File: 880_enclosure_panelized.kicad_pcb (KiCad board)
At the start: 4 copper layers, 279.5 x 38 mm, 161 parts, among them CON1 BARREL_JACK, J1 RUN/STOP, J10 RS IN, J11 CP IN, J12 MA IN, J13 CB IN, J14 CY IN, J15 OH IN, J16 CH IN, J17 IN 1, J18 IN 2, J19 IN 3, J2 SYNC24 CLK, J20 IN 4, J21 MULT IN, J22 SUM, J3 ASSIGN 1, J4 ASSIGN 2, J5 BD IN, J6 SD IN, J7 LT IN, J8 MT IN, J9 HT IN, P1 CONN_02X03, P2 CONN_01X02, P3 CONN_02X08, P4 CONN_01X03, P5 CONN_01X04, P7 CONN_01X03, Q1 MMBT3904, Q10 MMBT3904, Q11 MMBT3904, Q12 MMBT3904, Q14 C945, Q15 A733, Q2 MMBT3904, Q3 MMBT3904, Q4 MMBT3904, Q5 MMBT3904, Q6 MMBT3904, Q7 MMBT3904, Q8 MMBT3904, Q9 MMBT3904, U1 74HC165, U2 74HC165, U3 VX078-500, U4 VX078-500, U5 4558, U6 4558, U7 74HC1G125, X1 MIDI OUT, X2 SYNC24

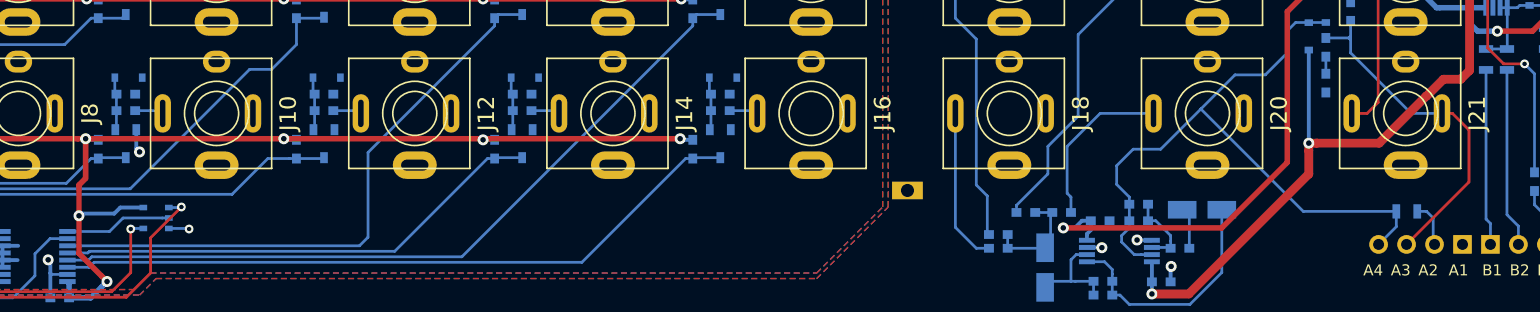
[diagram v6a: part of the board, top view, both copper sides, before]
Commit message: 4 layer, added tri-state buffer on MISO line, ordered prototype PCB
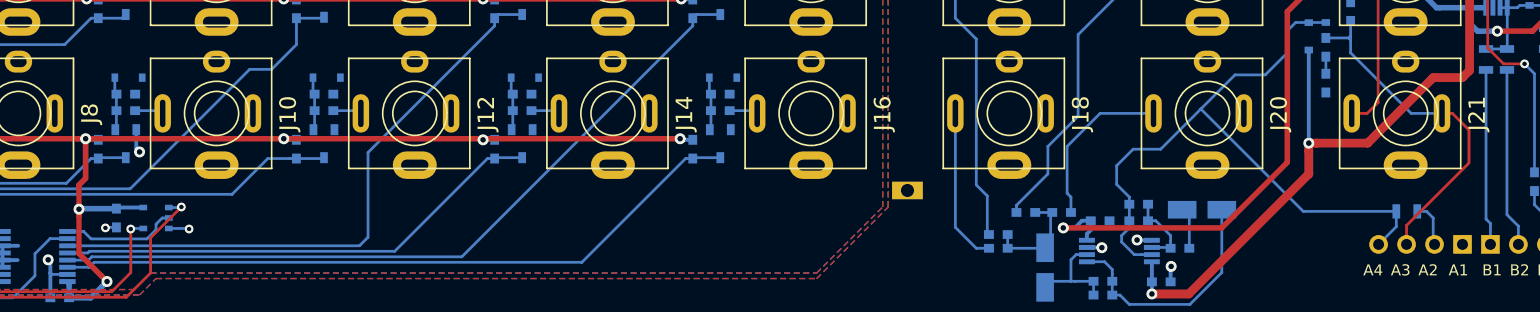
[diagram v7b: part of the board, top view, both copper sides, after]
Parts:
- added C20: 0.1µ, MyModules:SM0603-C-MURATA, B.Cu at (141.9, 86.5)
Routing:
- net GNDD: track 78.9 -> 79.9 mm, vias 6 -> 7
- net Net-(U2-Pad9): track 9.74 -> 10.6 mm
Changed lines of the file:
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@@
 (kicad_pcb (version 4) (host pcbnew 4.0.2-stable)
   (general
-    (links 349)
+    (links 351)
     (no_connects 0)
-    (area 11.944431 57.449999 291.550001 95.551147)
+    (area 9.341667 55.389285 291.550001 97.0016)
     (thickness 1.6)
     (drawings 115)
-    (tracks 798)
+    (tracks 804)
     (zones 0)
-    (modules 161)
+    (modules 162)
     (nets 111)
   )
@@
     (35 F.Paste user)
     (36 B.SilkS user)
-    (37 F.SilkS user hide)
+    (37 F.SilkS user)
     (38 B.Mask user)
     (39 F.Mask user)
@@
   )
   (setup
-    (last_trace_width 0.35)
+    (last_trace_width 0.25)
     (user_trace_width 0.25)
     (user_trace_width 0.35)
@@
     (visible_elements 7FFFF77F)
     (pcbplotparams
-      (layerselection 0x010f0_80000001)
+      (layerselection 0x010f0_80000007)
       (usegerberextensions true)
       (excludeedgelayer true)
@@
       (drillshape 0)
       (scaleselection 1)
-      (outputdirectory Gerbers/))
+      (outputdirectory Gerbers/r1.2/))
   )
   (net 0 "")
@@
     )
   )
+  (module MyModules:SM0603-C-MURATA (layer B.Cu)
+    (at 141.9 86.5 270)
+    (attr smd)
+    (fp_text reference C20 (at 0 1.4 270) (layer B.SilkS)
+      (effects (font (size 0.6096 0.6096) (thickness 0.1524)) (justify mirror))
+    )
+    (fp_text value 0.1µ (at 0 0 270) (layer B.SilkS) hide
+      (effects (font (size 0.508 0.4572) (thickness 0.1143)) (justify mirror))
+    )
+    (fp_line (start -0.5 0.5) (end 0.5 0.5) (layer B.SilkS) (width 0.2))
+    (fp_line (start -0.5 -0.5) (end 0.5 -0.5) (layer B.SilkS) (width 0.2))
+    (pad 1 smd rect (at -0.85 0 270) (size 0.9 0.8) (layers B.Cu B.Paste B.Mask)
+      (net 3 +5V))
+    (pad 2 smd rect (at 0.85 0 270) (size 0.9 0.8) (layers B.Cu B.Paste B.Mask)
+      (net 106 GNDD))
+    (model Capacitors_SMD.3dshapes/C_0603.wrl
+      (at (xyz 0 0 0.001))
+      (scale (xyz 1 1 1))
+      (rotate (xyz 0 0 0))
+    )
+  )
   (gr_text GND (at 75 92.5) (layer B.SilkS)
     (effects (font (size 0.8 0.8) (thickness 0.15)) (justify mirror))
@@
   (segment (start 30.4 83.3) (end 28.6 83.3) (width 0.35) (layer B.Cu) (net 2))
   (via (at 28.6 83.3) (size 1) (drill 0.5) (layers F.Cu B.Cu) (net 2))
+  (segment (start 138.5 83.5) (end 138.5 85.7) (width 0.5) (layer F.Cu) (net 3))
+  (segment (start 138.5 85.7) (end 138.5 86.3) (width 0.5) (layer F.Cu) (net 3))
+  (via (at 138.5 85.7) (size 1) (drill 0.5) (layers F.Cu B.Cu) (net 3))
+  (segment (start 141.9 85.65) (end 138.55 85.65) (width 0.5) (layer B.Cu) (net 3))
+  (segment (start 138.55 85.65) (end 138.5 85.7) (width 0.35) (layer B.Cu) (net 3))
+  (segment (start 144.34 85.55) (end 142 85.55) (width 0.35) (layer B.Cu) (net 3))
+  (segment (start 142 85.55) (end 141.9 85.65) (width 0.35) (layer B.Cu) (net 3))
   (segment (start 138.5 89.721069) (end 140.548913 91.769982) (width 0.5) (layer F.Cu) (net 3))
   (segment (start 140.548913 92.76998) (end 141.048912 92.269981) (width 0.5) (layer B.Cu) (net 3))
@@
   (segment (start 137.6 93.75) (end 137.6 92.425) (width 0.5) (layer B.Cu) (net 3))
   (segment (start 137.6 92.425) (end 137.525001 92.350001) (width 0.5) (layer B.Cu) (net 3))
-  (segment (start 138.5 83.5) (end 138.5 86.3) (width 0.5) (layer F.Cu) (net 3))
   (segment (start 139.1 79.3) (end 139.1 82.9) (width 0.5) (layer F.Cu) (net 3))
   (segment (start 139.1 82.9) (end 138.5 83.5) (width 0.5) (layer F.Cu) (net 3))
-  (segment (start 144.34 85.55) (end 142.25 85.55) (width 0.35) (layer B.Cu) (net 3))
-  (segment (start 142.25 85.55) (end 141.7 86.1) (width 0.35) (layer B.Cu) (net 3))
-  (segment (start 141.7 86.1) (end 138.7 86.1) (width 0.35) (layer B.Cu) (net 3))
-  (segment (start 138.7 86.1) (end 138.5 86.3) (width 0.35) (layer B.Cu) (net 3))
-  (via (at 138.5 86.3) (size 1) (drill 0.5) (layers F.Cu B.Cu) (net 3))
   (segment (start 120.5 76.7) (end 122.2 76.7) (width 0.8) (layer B.Cu) (net 3))
   (segment (start 122.2 76.7) (end 122.25 76.75) (width 0.35) (layer B.Cu) (net 3))
@@
   (segment (start 67.4505 88.9205) (end 67.53 89) (width 1) (layer B.Cu) (net 8))
   (segment (start 67.53 89) (end 70.95 89) (width 1) (layer B.Cu) (net 8))
+  (segment (start 271.500002 59.4) (end 267.4 59.4) (width 0.8) (layer F.Cu) (net 9))
+  (segment (start 267.4 59.4) (end 264.8 62) (width 0.8) (layer F.Cu) (net 9))
+  (segment (start 264.8 62) (end 264.8 73.1) (width 0.8) (layer F.Cu) (net 9))
+  (segment (start 264.8 73.1) (end 264.15 73.75) (width 0.8) (layer F.Cu) (net 9))
+  (segment (start 264.15 73.75) (end 261.5 73.75) (width 0.8) (layer F.Cu) (net 9))
+  (segment (start 261.5 73.75) (end 255.55 79.7) (width 0.8) (layer F.Cu) (net 9))
+  (segment (start 255.55 79.7) (end 250.907112 79.7) (width 0.8) (layer F.Cu) (net 9))
+  (segment (start 250.907112 79.7) (end 250.200006 79.7) (width 0.8) (layer F.Cu) (net 9))
   (segment (start 41.23 88.98) (end 41.23 87.27) (width 1) (layer In1.Cu) (net 9))
   (segment (start 70.8 83.4) (end 74.5 87.1) (width 1) (layer In1.Cu) (net 9))
@@
   (segment (start 29.1795 89.3205) (end 33.4 85.1) (width 1) (layer B.Cu) (net 9))
   (segment (start 33.4 85.1) (end 33.4 83.3) (width 1) (layer B.Cu) (net 9))
-  (segment (start 271.500002 59.4) (end 267.4 59.4) (width 0.8) (layer F.Cu) (net 9))
-  (segment (start 267.4 59.4) (end 264.8 62) (width 0.8) (layer F.Cu) (net 9))
-  (segment (start 264.8 62) (end 264.8 73.1) (width 0.8) (layer F.Cu) (net 9))
-  (segment (start 264.8 73.1) (end 264 73.9) (width 0.8) (layer F.Cu) (net 9))
-  (segment (start 264 73.9) (end 262.420087 73.9) (width 0.8) (layer F.Cu) (net 9))
-  (segment (start 262.420087 73.9) (end 260.89999 75.420097) (width 0.8) (layer F.Cu) (net 9))
-  (segment (start 260.89999 75.420097) (end 260.879903 75.420097) (width 0.8) (layer F.Cu) (net 9))
-  (segment (start 260.879903 75.420097) (end 256.6 79.7) (width 0.8) (layer F.Cu) (net 9))
-  (segment (start 256.6 79.7) (end 250.907112 79.7) (width 0.8) (layer F.Cu) (net 9))
-  (segment (start 250.907112 79.7) (end 250.200006 79.7) (width 0.8) (layer F.Cu) (net 9))
   (segment (start 250.200006 82.5071) (end 250.200006 80.407106) (width 0.8) (layer F.Cu) (net 9))
   (segment (start 250.200006 80.407106) (end 250.200006 79.7) (width 0.8) (layer F.Cu) (net 9))
@@
   (segment (start 262.3 77) (end 263.25 77) (width 0.25) (layer F.Cu) (net 96))
   (segment (start 263.25 77) (end 264.75 78.5) (width 0.25) (layer F.Cu) (net 96))
-  (segment (start 264.75 78.5) (end 264.75 83.23) (width 0.25) (layer F.Cu) (net 96))
-  (segment (start 264.75 83.23) (end 259.08 88.9) (width 0.25) (layer F.Cu) (net 96))
+  (segment (start 264.75 78.5) (end 264.75 81.5) (width 0.25) (layer F.Cu) (net 96))
+  (segment (start 264.75 81.5) (end 259.08 87.17) (width 0.25) (layer F.Cu) (net 96))
+  (segment (start 259.08 87.17) (end 259.08 88.9) (width 0.25) (layer F.Cu) (net 96))
   (segment (start 254 71.5) (end 254 70.3) (width 0.25) (layer B.Cu) (net 96))
   (segment (start 254 70.3) (end 254 70) (width 0.25) (layer B.Cu) (net 96))
@@
   (segment (start 268.2 86.2) (end 269.24 87.24) (width 0.25) (layer B.Cu) (net 99))
   (segment (start 269.24 87.24) (end 269.24 88.9) (width 0.25) (layer B.Cu) (net 99))
+  (segment (start 141.9 87.35) (end 140.95 87.35) (width 0.25) (layer B.Cu) (net 106))
+  (segment (start 140.95 87.35) (end 140.9 87.4) (width 0.25) (layer B.Cu) (net 106))
+  (via (at 140.9 87.4) (size 0.8) (drill 0.4) (layers F.Cu B.Cu) (net 106))
   (segment (start 40.5 79.3) (end 39.729081 78.529081) (width 0.25) (layer F.Cu) (net 106))
   (segment (start 43.4 79.3) (end 40.5 79.3) (width 0.25) (layer F.Cu) (net 106))
@@
   (segment (start 237.65 88.6) (end 237.65 89.25) (width 0.25) (layer B.Cu) (net 107))
   (segment (start 235.6 86.75) (end 235.6 85.25) (width 0.25) (layer B.Cu) (net 107))
-  (segment (start 137.45 87.725) (end 141.275 87.725) (width 0.25) (layer B.Cu) (net 110))
-  (segment (start 141.275 87.725) (end 142.5 86.5) (width 0.25) (layer B.Cu) (net 110))
-  (segment (start 142.5 86.5) (end 146.06 86.5) (width 0.25) (layer B.Cu) (net 110))
-  (segment (start 146.06 86.5) (end 146.66 86.5) (width 0.25) (layer B.Cu) (net 110))
+  (segment (start 146.66 86.5) (end 146.06 86.5) (width 0.25) (layer B.Cu) (net 110))
+  (segment (start 146.06 86.5) (end 145.5 87.06) (width 0.25) (layer B.Cu) (net 110))
+  (segment (start 145.5 87.06) (end 145.5 87.570002) (width 0.25) (layer B.Cu) (net 110))
+  (segment (start 145.5 87.570002) (end 144.670002 88.4) (width 0.25) (layer B.Cu) (net 110))
+  (segment (start 138.925 87.725) (end 137.45 87.725) (width 0.25) (layer B.Cu) (net 110))
+  (segment (start 144.670002 88.4) (end 139.6 88.4) (width 0.25) (layer B.Cu) (net 110))
+  (segment (start 139.6 88.4) (end 138.925 87.725) (width 0.25) (layer B.Cu) (net 110))
   (segment (start 136.949992 87.75) (end 136.949992 87.725) (width 0.25) (layer B.Cu) (net 110))
   (zone (net 16) (net_name "Net-(CON1-Pad1)") (layer B.Cu) (hatch edge 0.508)

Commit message: few tweaks before panelizing. kept 74HCT1G125GV footprint as TSOP-5-SC74A-SOT-753, which is the larger of the two available footprints for U7
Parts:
- added R44: 47K, MyModules:SM0603-R-YAGEO, B.Cu at (142.4, 86.5)
- added R45: 47K, MyModules:SM0603-R-YAGEO, B.Cu at (151.8, 87.5)
- moved C20 1.00 mm to (140.9, 86.5)
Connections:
- P7 pad 3: /PHONE_GND -> GND
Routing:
- net GND: track 31.1 -> 51.2 mm, vias 12 -> 13
- net -V: track 295.3 -> 279.0 mm
- net ISP_MISO: track 27.4 -> 41.5 mm, vias 1 -> 2
- net Net-(CON1-Pad1): track 0.00 -> 4.31 mm
- net Net-(D17-Pad2): track 3.86 -> 0.06 mm
- net Net-(J21-Pad2): track 32.1 -> 29.6 mm
- net Net-(R57-Pad2): track 24.9 -> 22.8 mm
- net +V: track 310.1 -> 309.5 mm
- net Net-(R1-Pad1): track 51.6 -> 51.0 mm
- added copper zone on B.Cu, net +V
- added copper zone on B.Cu, net -V
- added copper zone on B.Cu, net Net-(C4-Pad1)
- added copper zone on B.Cu, net Net-(C5-Pad1)
- added copper zone on B.Cu, net Net-(C6-Pad2)
- added copper zone on B.Cu, net Net-(C7-Pad1)
- added copper zone on B.Cu, net Net-(C8-Pad2)
- added copper zone on B.Cu, net Net-(D17-Pad2)
